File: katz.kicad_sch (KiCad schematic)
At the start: 62 parts, among them SW1 choc_SW_HS, SW10 choc_SW_HS, SW11 choc_SW_HS, SW12 choc_SW_HS, SW13 choc_SW_HS, SW14 choc_SW_HS, SW15 choc_SW_HS, SW16 choc_SW_HS, SW17 choc_SW_HS, SW18 choc_SW_HS, SW19 choc_SW_HS, SW2 choc_SW_HS, SW20 choc_SW_HS, SW21 choc_SW_HS, SW22 choc_SW_HS, SW23 choc_SW_HS, SW24 choc_SW_HS, SW25 choc_SW_HS, SW26 choc_SW_HS, SW27 choc_SW_HS, SW28 choc_SW_HS, SW29 choc_SW_HS, SW3 choc_SW_HS, SW30 choc_SW_HS, SW4 choc_SW_HS, SW5 choc_SW_HS, SW6 choc_SW_HS, SW7 choc_SW_HS, SW8 choc_SW_HS, SW9 choc_SW_HS, U1 SeeeduinoXIAO

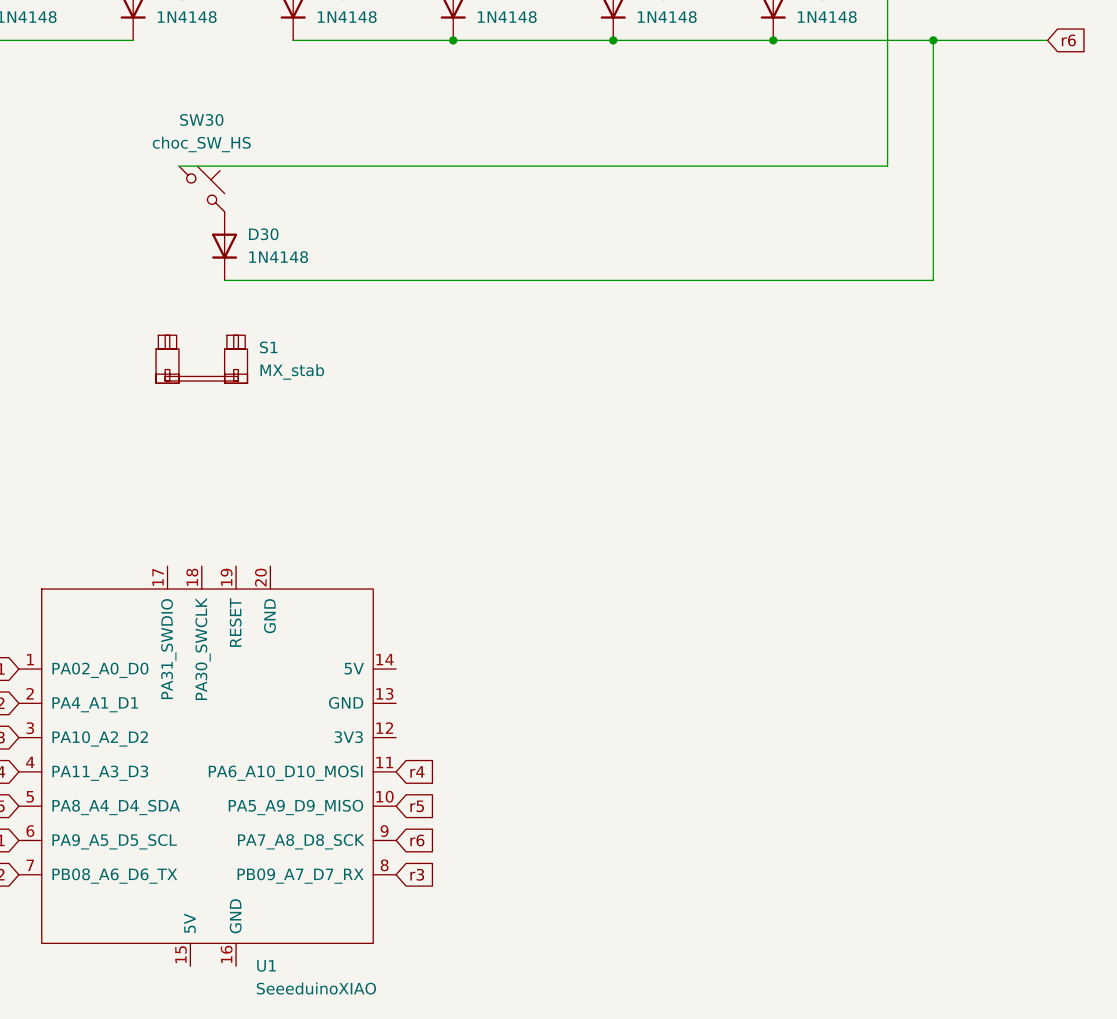
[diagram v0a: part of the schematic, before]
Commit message: add pins to removable space bar
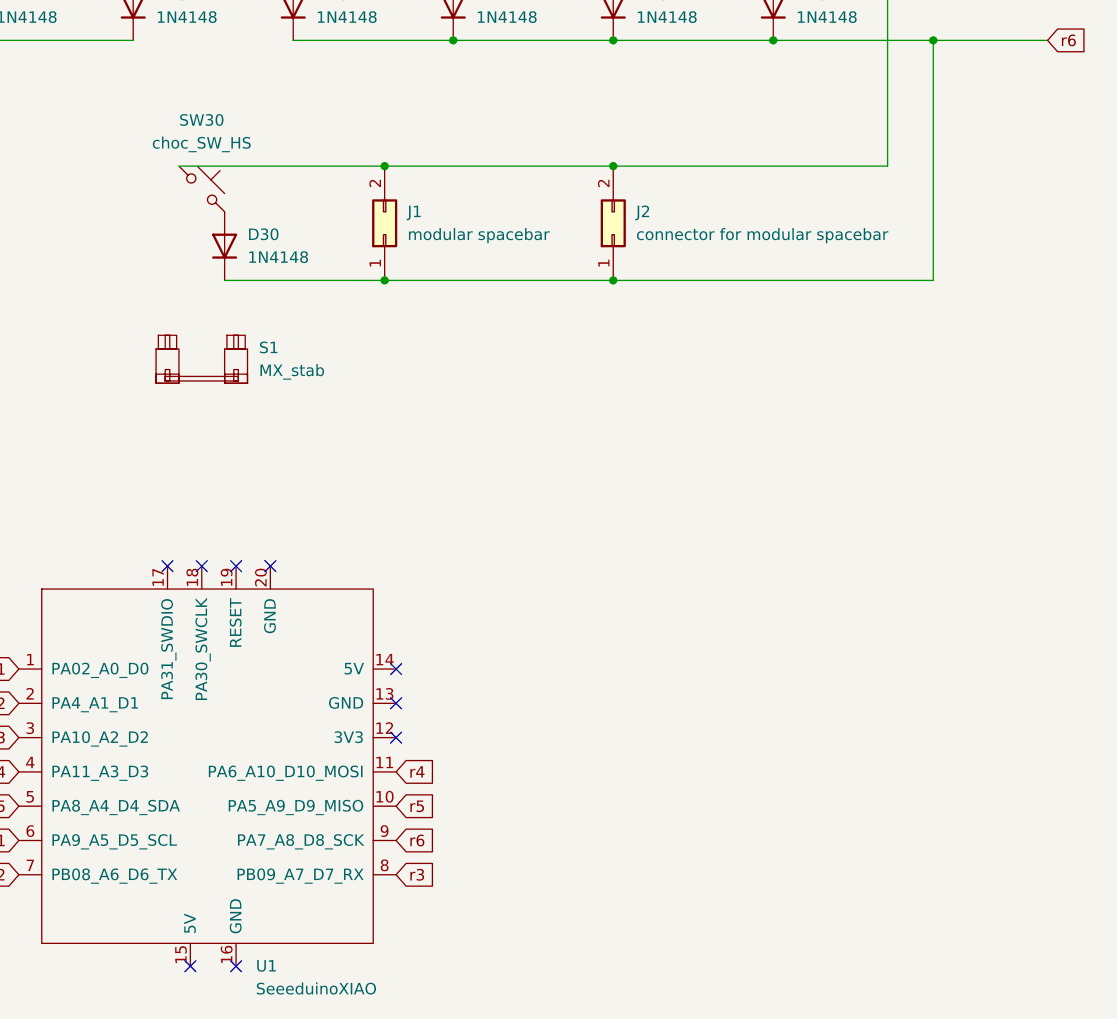
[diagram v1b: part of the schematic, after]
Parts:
- added J1: modular spacebar, Connector_PinHeader_2.54mm:PinHeader_2x01_P2.54mm_Vertical, symbol Connector_Generic:Conn_02x01
- added J2: connector for modular spacebar, Connector_PinHeader_2.54mm:PinHeader_2x01_P2.54mm_Vertical, symbol Connector_Generic:Conn_02x01
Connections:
- net c1: now also J1.2 (Pin_2), J2.2 (Pin_2)
- net r6: now also J1.1 (Pin_1), J2.1 (Pin_1)
- no-connect marks 0 -> 9
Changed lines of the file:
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@@
   (junction (at 57.15 72.39) (diameter 0) (color 0 0 0 0)
   )
+  (junction (at 138.43 113.03) (diameter 0) (color 0 0 0 0)
+  )
   (junction (at 74.93 99.06) (diameter 0) (color 0 0 0 0)
   )
@@
   (junction (at 140.97 59.69) (diameter 0) (color 0 0 0 0)
   )
+  (junction (at 138.43 125.73) (diameter 0) (color 0 0 0 0)
+  )
   (junction (at 123.19 33.02) (diameter 0) (color 0 0 0 0)
   )
@@
   (junction (at 199.39 45.72) (diameter 0) (color 0 0 0 0)
   )
+  (junction (at 163.83 113.03) (diameter 0) (color 0 0 0 0)
+  )
   (junction (at 199.39 99.06) (diameter 0) (color 0 0 0 0)
   )
@@
   (junction (at 74.93 45.72) (diameter 0) (color 0 0 0 0)
   )
+  (junction (at 163.83 125.73) (diameter 0) (color 0 0 0 0)
+  )
   (junction (at 194.31 59.69) (diameter 0) (color 0 0 0 0)
   )
   (junction (at 105.41 33.02) (diameter 0) (color 0 0 0 0)
   )
+  (no_connect (at 116.84 201.93))
+  (no_connect (at 121.92 157.48))
+  (no_connect (at 121.92 201.93))
+  (no_connect (at 139.7 176.53))
+  (no_connect (at 114.3 157.48))
+  (no_connect (at 139.7 168.91))
+  (no_connect (at 139.7 172.72))
+  (no_connect (at 125.73 157.48))
+  (no_connect (at 118.11 157.48))
+  (wire (pts (xy 163.83 113.03) (xy 194.31 113.03))
+    (stroke (width 0) (type default))
+  )
   (wire (pts (xy 92.71 99.06) (xy 110.49 99.06))
     (stroke (width 0) (type default))
@@
     (stroke (width 0) (type default))
   )
+  (wire (pts (xy 138.43 125.73) (xy 163.83 125.73))
+    (stroke (width 0) (type default))
+  )
   (wire (pts (xy 123.19 25.4) (xy 123.19 33.02))
     (stroke (width 0) (type default))
@@
     (stroke (width 0) (type default))
   )
+  (wire (pts (xy 138.43 113.03) (xy 115.57 113.03))
+    (stroke (width 0) (type default))
+  )
   (wire (pts (xy 140.97 59.69) (xy 140.97 86.36))
     (stroke (width 0) (type default))
@@
     (stroke (width 0) (type default))
   )
+  (wire (pts (xy 138.43 113.03) (xy 163.83 113.03))
+    (stroke (width 0) (type default))
+  )
   (wire (pts (xy 39.37 72.39) (xy 57.15 72.39))
     (stroke (width 0) (type default))
@@
     (stroke (width 0) (type default))
   )
+  (wire (pts (xy 163.83 125.73) (xy 199.39 125.73))
+    (stroke (width 0) (type default))
+  )
   (wire (pts (xy 176.53 25.4) (xy 176.53 33.02))
     (stroke (width 0) (type default))
@@
     (stroke (width 0) (type default))
   )
-  (wire (pts (xy 120.65 125.73) (xy 199.39 125.73))
+  (wire (pts (xy 120.65 125.73) (xy 138.43 125.73))
     (stroke (width 0) (type default))
   )
@@
   )
   (wire (pts (xy 194.31 33.02) (xy 194.31 59.69))
-    (stroke (width 0) (type default))
-  )
-  (wire (pts (xy 194.31 113.03) (xy 115.57 113.03))
     (stroke (width 0) (type default))
   )
@@
     )
   )
+  (symbol (lib_id "Connector_Generic:Conn_02x01") (at 163.83 120.65 90) (unit 1)
+    (in_bom yes) (on_board yes) (dnp no) (fields_autoplaced)
+    (property "Reference" "J2" (at 166.37 118.11 90)
+      (effects (font (size 1.27 1.27)) (justify right))
+    )
+    (property "Value" "connector for modular spacebar" (at 166.37 120.65 90)
+      (effects (font (size 1.27 1.27)) (justify right))
+    )
+    (property "Footprint" "Connector_PinHeader_2.54mm:PinHeader_2x01_P2.54mm_Vertical" (at 163.83 120.65 0)
+      (effects (font (size 1.27 1.27)) hide)
+    )
+    (property "Datasheet" "~" (at 163.83 120.65 0)
+      (effects (font (size 1.27 1.27)) hide)
+    )
+    (pin "1")
+    (pin "2")
+    (instances
+      (project "katz"
+        (path "/777e27e0-09ef-49c6-aecd-cda8c0a5c397"
+          (reference "J2") (unit 1)
+        )
+      )
+    )
+  )
   (symbol (lib_id "Diode:1N4148") (at 110.49 95.25 90) (unit 1)
     (in_bom yes) (on_board yes) (dnp no) (fields_autoplaced)
@@
         )
       )
+    )
+  )
+  (symbol (lib_id "Connector_Generic:Conn_02x01") (at 138.43 120.65 90) (unit 1)
+    (in_bom yes) (on_board yes) (dnp no) (fields_autoplaced)
+    (property "Reference" "J1" (at 140.97 118.11 90)
+      (effects (font (size 1.27 1.27)) (justify right))
+    )
+    (property "Value" "modular spacebar" (at 140.97 120.65 90)
+      (effects (font (size 1.27 1.27)) (justify right))
+    )
+    (property "Footprint" "Connector_PinHeader_2.54mm:PinHeader_2x01_P2.54mm_Vertical" (at 138.43 120.65 0)
+      (effects (font (size 1.27 1.27)) hide)
+    )
+    (property "Datasheet" "~" (at 138.43 120.65 0)
+      (effects (font (size 1.27 1.27)) hide)
+    )
+    (pin "1")
+    (pin "2")
+    (instances
+      (project "katz"
+        (path "/777e27e0-09ef-49c6-aecd-cda8c0a5c397"
+          (reference "J1") (unit 1)
+        )
+      )
